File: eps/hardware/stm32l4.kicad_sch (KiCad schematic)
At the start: 32 parts, among them J9 Conn_02x03_Odd_Even, SW1 SW_Push_Dual, SW2 SW_SPDT, U10 STM32L496ZGTx, Y1 8Mhz, Y2 32KHz

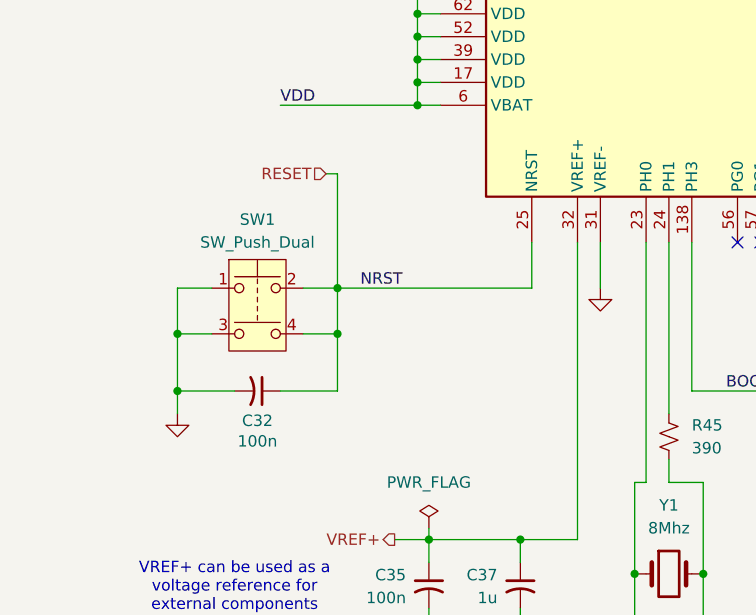
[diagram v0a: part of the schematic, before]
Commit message: fix all but one warning
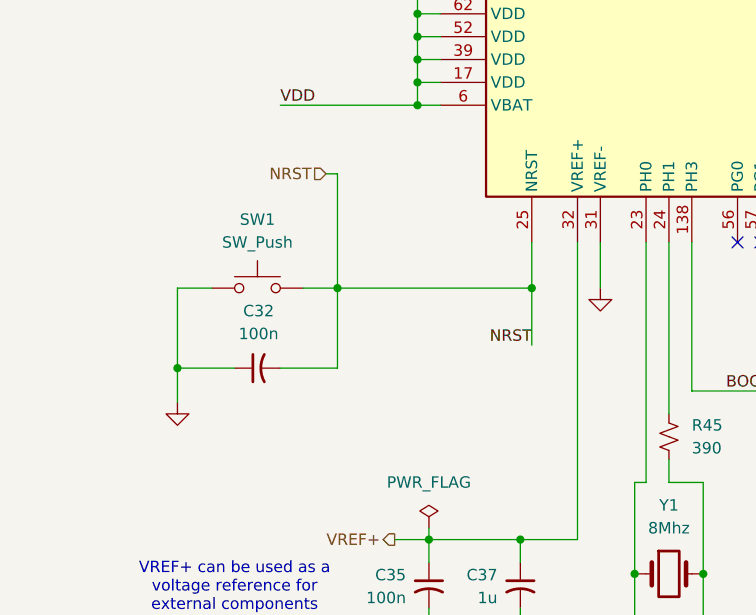
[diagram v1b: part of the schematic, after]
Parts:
- SW1: value SW_Push_Dual -> SW_Push; symbol Switch:SW_Push_Dual -> Switch:SW_Push
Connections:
- net GND: now also C32.1; no longer C32.2, SW1.3
- net RESET renamed NRST
- net NRST: now also C32.2; no longer C32.1, SW1.4

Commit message: netlist fixes
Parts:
- renumbered R45 to R33, R46 to R34
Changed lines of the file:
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@@
 		(dnp no)
 		(fields_autoplaced yes)
-		(property "Reference" "R45"
+		(property "Reference" "R33"
 			(at 85.09 157.4799 0)
 			(effects
@@
 			(project "eps"
 				(path "/9e0ae2e7-d4be-41b4-8312-0d2aceea2180/01f97f68-bf84-46d4-bbb8-12ed1320856d"
-					(reference "R45")
+					(reference "R33")
 					(unit 1)
 				)
@@
 		(dnp no)
 		(fields_autoplaced yes)
-		(property "Reference" "#FLG04"
+		(property "Reference" "#FLG05"
 			(at 55.88 167.005 0)
 			(effects
@@
 			(project ""
 				(path "/9e0ae2e7-d4be-41b4-8312-0d2aceea2180/01f97f68-bf84-46d4-bbb8-12ed1320856d"
-					(reference "#FLG04")
+					(reference "#FLG05")
 					(unit 1)
 				)
@@
 		(dnp no)
 		(fields_autoplaced yes)
-		(property "Reference" "R46"
+		(property "Reference" "R34"
 			(at 101.6 156.2099 0)
 			(effects
@@
 			(project ""
 				(path "/9e0ae2e7-d4be-41b4-8312-0d2aceea2180/01f97f68-bf84-46d4-bbb8-12ed1320856d"
-					(reference "R46")
+					(reference "R34")
 					(unit 1)
 				)
@@
 		(dnp no)
 		(fields_autoplaced yes)
-		(property "Reference" "#FLG05"
+		(property "Reference" "#FLG06"
 			(at 190.5 22.225 0)
 			(effects
@@
 			(project ""
 				(path "/9e0ae2e7-d4be-41b4-8312-0d2aceea2180/01f97f68-bf84-46d4-bbb8-12ed1320856d"
-					(reference "#FLG05")
-					(unit 1)
-				)
+					(reference "#FLG06")
+					(unit 1)
+				)

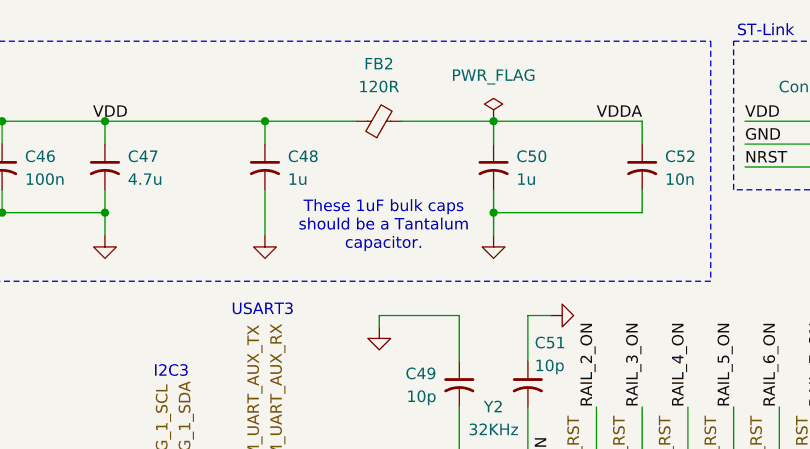
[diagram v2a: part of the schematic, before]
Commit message: start footprint assignment
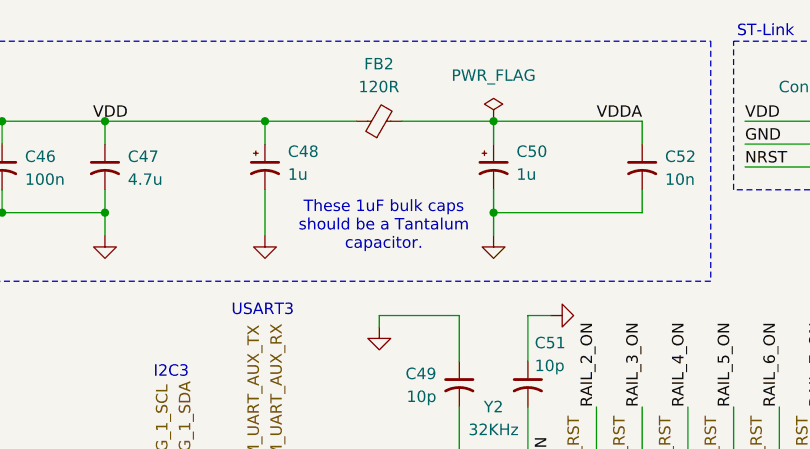
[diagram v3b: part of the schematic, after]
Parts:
- C30, C31, C32, C33, C34, C35, C36, C37, C38, C39, C40, C41, C42, C43, C44, C45, C46, C47, C49, C51, C52: footprint (none) -> Capacitor_SMD:C_0603_1608Metric
- C48, C50: footprint (none) -> Capacitor_Tantalum_SMD:CP_EIA-3216-18_Kemet-A; symbol Device:C_Small_US -> Device:C_Polarized_Small_US
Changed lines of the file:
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@@
 			)
 		)
-		(property "Footprint" ""
+		(property "Footprint" "Capacitor_SMD:C_0603_1608Metric"
 			(at 147.32 29.21 0)
 			(effects
@@
 			)
 		)
-		(property "Footprint" ""
+		(property "Footprint" "Capacitor_SMD:C_0603_1608Metric"
 			(at 105.41 29.21 0)
 			(effects
@@
 			)
 		)
-		(property "Footprint" ""
+		(property "Footprint" "Capacitor_SMD:C_0603_1608Metric"
 			(at 36.83 151.13 0)
 			(effects
@@
 	)
 	(symbol
-		(lib_id "Device:C_Small_US")
+		(lib_id "Device:C_Polarized_Small_US")
 		(at 165.1 29.21 0)
 		(unit 1)
@@
 		(fields_autoplaced yes)
 		(property "Reference" "C48"
-			(at 167.64 28.0669 0)
+			(at 167.64 27.5081 0)
 			(effects
 				(font
@@
 		)
 		(property "Value" "1u"
-			(at 167.64 30.6069 0)
+			(at 167.64 30.0481 0)
 			(effects
 				(font
@@
 			)
 		)
-		(property "Footprint" ""
+		(property "Footprint" "Capacitor_Tantalum_SMD:CP_EIA-3216-18_Kemet-A"
 			(at 165.1 29.21 0)
 			(effects
@@
 			)
 		)
-		(property "Datasheet" ""
+		(property "Datasheet" "~"
 			(at 165.1 29.21 0)
 			(effects
@@
 			)
 		)
-		(property "Description" "capacitor, small US symbol"
+		(property "Description" "Polarized capacitor, small US symbol"
 			(at 165.1 29.21 0)
 			(effects
@@
 			)
 		)
-		(property "Footprint" ""
+		(property "Footprint" "Capacitor_SMD:C_0603_1608Metric"
 			(at 34.29 29.21 0)
 			(effects
@@
 			)
 		)
-		(property "Footprint" ""
+		(property "Footprint" "Capacitor_SMD:C_0603_1608Metric"
 			(at 86.36 186.69 0)
 			(effects
@@
 			)
 		)
-		(property "Footprint" ""
+		(property "Footprint" "Capacitor_SMD:C_0603_1608Metric"
 			(at 95.25 29.21 0)
 			(effects
@@
 			)
 		)
-		(property "Footprint" ""
+		(property "Footprint" "Capacitor_SMD:C_0603_1608Metric"
 			(at 186.69 53.34 0)
 			(effects
@@
 			)
 		)
-		(property "Footprint" ""
+		(property "Footprint" "Capacitor_SMD:C_0603_1608Metric"
 			(at 85.09 29.21 0)
 			(effects
@@
 			)
 		)
-		(property "Footprint" ""
+		(property "Footprint" "Capacitor_SMD:C_0603_1608Metric"
 			(at 74.93 29.21 0)
 			(effects
@@
 			)
 		)
-		(property "Footprint" ""
+		(property "Footprint" "Capacitor_SMD:C_0603_1608Metric"
 			(at 55.88 175.26 0)
 			(effects
@@
 			)
 		)
-		(property "Footprint" ""
+		(property "Footprint" "Capacitor_SMD:C_0603_1608Metric"
 			(at 207.01 29.21 0)
 			(effects
@@
 			)
 		)
-		(property "Footprint" ""
+		(property "Footprint" "Capacitor_SMD:C_0603_1608Metric"
 			(at 125.73 29.21 0)
 			(effects
@@
 			)
 		)
-		(property "Footprint" ""
+		(property "Footprint" "Capacitor_SMD:C_0603_1608Metric"
 			(at 78.74 186.69 0)
 			(effects
@@
 			)
 		)
-		(property "Footprint" ""
+		(property "Footprint" "Capacitor_SMD:C_0603_1608Metric"
 			(at 54.61 29.21 0)
 			(effects
@@
 			)
 		)
-		(property "Footprint" ""
+		(property "Footprint" "Capacitor_SMD:C_0603_1608Metric"
 			(at 135.89 29.21 0)
 			(effects
@@
 			)
 		)
-		(property "Footprint" ""
+		(property "Footprint" "Capacitor_SMD:C_0603_1608Metric"
 			(at 64.77 29.21 0)
 			(effects
@@
 			)
 		)
-		(property "Footprint" ""
+		(property "Footprint" "Capacitor_SMD:C_0603_1608Metric"
 			(at 66.04 175.26 0)
 			(effects
@@
 			)
 		)
-		(property "Footprint" ""
+		(property "Footprint" "Capacitor_SMD:C_0603_1608Metric"
 			(at 194.31 53.34 0)
 			(effects
@@
 	)
 	(symbol
-		(lib_id "Device:C_Small_US")
+		(lib_id "Device:C_Polarized_Small_US")
 		(at 190.5 29.21 0)
 		(unit 1)
@@
 		(fields_autoplaced yes)
 		(property "Reference" "C50"
-			(at 193.04 28.0669 0)
+			(at 193.04 27.5081 0)
 			(effects
 				(font
@@
 		)
 		(property "Value" "1u"
-			(at 193.04 30.6069 0)
+			(at 193.04 30.0481 0)
 			(effects
 				(font
@@
 			)
 		)
-		(property "Footprint" ""
+		(property "Footprint" "Capacitor_Tantalum_SMD:CP_EIA-3216-18_Kemet-A"
 			(at 190.5 29.21 0)
 			(effects
@@
 			)
 		)
-		(property "Datasheet" ""
+		(property "Datasheet" "~"
 			(at 190.5 29.21 0)
 			(effects
@@
 			)
 		)
-		(property "Description" "capacitor, small US symbol"
+		(property "Description" "Polarized capacitor, small US symbol"
 			(at 190.5 29.21 0)
 			(effects
@@
 			)
 		)
-		(property "Footprint" ""
+		(property "Footprint" "Capacitor_SMD:C_0603_1608Metric"
 			(at 24.13 29.21 0)
 			(effects
@@
 			)
 		)
-		(property "Footprint" ""
+		(property "Footprint" "Capacitor_SMD:C_0603_1608Metric"
 			(at 44.45 29.21 0)
 			(effects
@@
 			)
 		)
-		(property "Footprint" ""
+		(property "Footprint" "Capacitor_SMD:C_0603_1608Metric"
 			(at 115.57 29.21 0)
 			(effects

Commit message: finish footprint assignment and board setup
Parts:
- removed Y1: 8Mhz, symbol Device:Crystal
- added Y1: 8MHz, Crystal:Crystal_SMD_3225-4Pin_3.2x2.5mm, symbol Device:Crystal_GND24
- FB2: footprint (none) -> Inductor_SMD:L_0603_1608Metric
- J9: footprint (none) -> Connector_PinHeader_2.54mm:PinHeader_2x03_P2.54mm_Vertical
- R33, R34: footprint (none) -> Resistor_SMD:R_0603_1608Metric
- SW1: footprint (none) -> Button_Switch_SMD:SW_Push_SPST_NO_Alps_SKRK
- SW2: footprint (none) -> Button_Switch_SMD:SW_SPDT_PCM12
- Y2: footprint (none) -> Crystal:Crystal_SMD_3215-2Pin_3.2x1.5mm
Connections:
- net GND: now also Y1.2, Y1.4
- net at C39.1, U10.23 (PH0): now also Y1.1
- net at C41.1, R33.2: now also Y1.3
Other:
- moved on the sheet: C39

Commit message: schematic fixes
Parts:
- removed J9: Conn_02x03_Odd_Even, Connector_PinHeader_2.54mm:PinHeader_2x03_P2.54mm_Vertical, symbol Connector_Generic:Conn_02x03_Odd_Even
- added J13: Conn_ARM_JTAG_SWD_10, Connector_PinHeader_1.27mm:PinHeader_2x05_P1.27mm_Vertical_SMD, symbol Connector:Conn_ARM_JTAG_SWD_10
- C30, C31, C32, C33, C34, C35, C36, C37, C38, C39, C40, C41, C42, C43, C44, C45, C46, C47, C49, C51, C52: footprint Capacitor_SMD:C_0603_1608Metric -> Capacitor_SMD:C_0402_1005Metric
- R33, R34: footprint Resistor_SMD:R_0603_1608Metric -> Resistor_SMD:R_0402_1005Metric
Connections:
- net GND: now also J13.3 (GND), J13.5 (GND), J13.9 (GNDDetect)
- net NRST: now also J13.10 (~{RESET})
- net SWCLK: now also J13.4 (SWCLK/TCK)
- net SWDIO: now also J13.2 (SWDIO/TMS)
- net VDD: now also J13.1 (VTref)
- no-connect marks 45 -> 46
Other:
- note added: "ADC RC Filters"

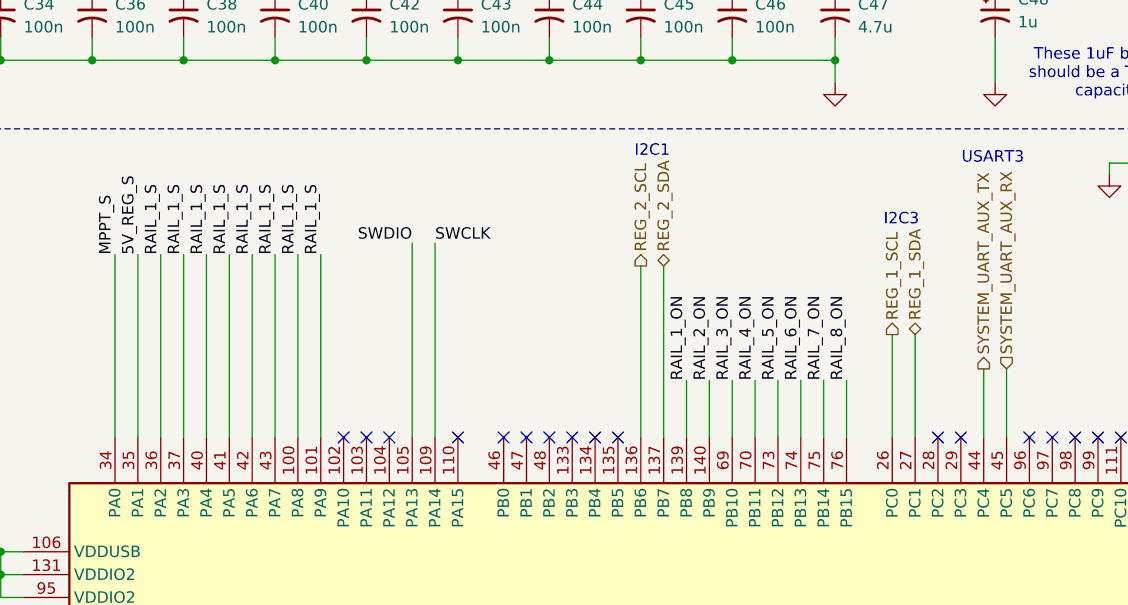
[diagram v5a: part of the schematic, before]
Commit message: finish rc filter passive placement & start other passives
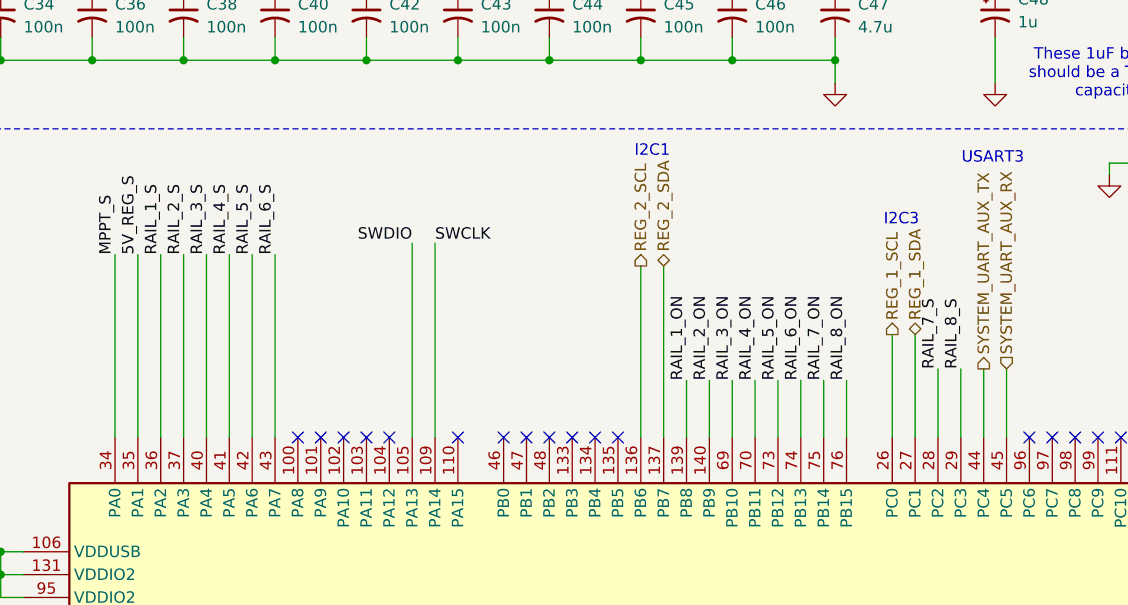
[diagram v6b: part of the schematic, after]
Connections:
- net RAIL_1_S: no longer U10.100 (PA8), U10.101 (PA9), U10.37 (PA3), U10.40 (PA4), U10.41 (PA5), U10.42 (PA6), U10.43 (PA7)
- net RAIL_2_S: now also U10.37 (PA3)
- net RAIL_3_S: now also U10.40 (PA4)
- net RAIL_4_S: now also U10.41 (PA5)
- net RAIL_5_S: now also U10.42 (PA6)
- net RAIL_6_S: now also U10.43 (PA7)
- net RAIL_7_S: now also U10.28 (PC2)
- net RAIL_8_S: now also U10.29 (PC3)
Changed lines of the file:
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@@
-	)
-	(no_connect
-		(at 158.75 76.2)
 	)
 	(no_connect
@@
 	)
 	(no_connect
+		(at 87.63 76.2)
+	)
+	(no_connect
 		(at 207.01 137.16)
 	)
@@
 	)
 	(no_connect
-		(at 161.29 76.2)
-	)
-	(no_connect
 		(at 186.69 76.2)
 	)
@@
 	)
 	(no_connect
+		(at 90.17 76.2)
+	)
+	(no_connect
 		(at 120.65 137.16)
 	)
@@
 	(wire
 		(pts
+			(xy 161.29 68.58) (xy 161.29 76.2)
+		)
+		(stroke
+			(width 0)
+			(type default)
+		)
+	)
+	(wire
+		(pts
 			(xy 64.77 34.29) (xy 74.93 34.29)
 		)
@@
 	(wire
 		(pts
-			(xy 87.63 55.88) (xy 87.63 76.2)
-		)
-		(stroke
-			(width 0)
-			(type default)
-		)
-	)
-	(wire
-		(pts
 			(xy 54.61 93.98) (xy 54.61 91.44)
 		)
@@
 	(wire
 		(pts
+			(xy 158.75 68.58) (xy 158.75 76.2)
+		)
+		(stroke
+			(width 0)
+			(type default)
+		)
+	)
+	(wire
+		(pts
 			(xy 54.61 116.84) (xy 54.61 119.38)
 		)
@@
 		(pts
 			(xy 146.05 69.85) (xy 146.05 76.2)
-		)
-		(stroke
-			(width 0)
-			(type default)
-		)
-	)
-	(wire
-		(pts
-			(xy 90.17 55.88) (xy 90.17 76.2)
 		)
 		(stroke
@@
 		)
 	)
-	(label "RAIL_1_S"
+	(label "RAIL_6_S"
 		(at 85.09 55.88 90)
 		(effects
@@
 		)
 	)
-	(label "RAIL_1_S"
+	(label "RAIL_3_S"
 		(at 77.47 55.88 90)
 		(effects
@@
 		)
 	)
+	(label "RAIL_8_S"
+		(at 161.29 68.58 90)
+		(effects
+			(font
+				(size 1.27 1.27)
+			)
+			(justify left bottom)
+		)
+	)
 	(label "VDDA"
 		(at 39.37 96.52 0)
@@
 		)
 	)
-	(label "RAIL_1_S"
+	(label "RAIL_2_S"
 		(at 74.93 55.88 90)
 		(effects
@@
 		)
 	)
-	(label "RAIL_1_S"
+	(label "RAIL_4_S"
 		(at 80.01 55.88 90)
 		(effects
@@
 		)
 	)
-	(label "RAIL_1_S"
-		(at 90.17 55.88 90)
-		(effects
-			(font
-				(size 1.27 1.27)
-			)
-			(justify left bottom)
-		)
-	)
-	(label "RAIL_1_S"
+	(label "RAIL_5_S"
 		(at 82.55 55.88 90)
 		(effects
@@
 		)
 	)
-	(label "RAIL_1_S"
-		(at 87.63 55.88 90)
-		(effects
-			(font
-				(size 1.27 1.27)
-			)
-			(justify left bottom)
-		)
-	)
 	(label "RAIL_8_ON"
 		(at 148.59 69.85 90)
@@
 		(effects
 			(font
+				(size 1.27 1.27)
+			)
+			(justify left bottom)
+		)
+	)
+	(label "RAIL_7_S"
+		(at 158.75 68.58 90)
+		(effects
+			(font
